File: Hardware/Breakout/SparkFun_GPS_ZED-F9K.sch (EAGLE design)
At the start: 48 parts, among them J1 QWIIC_RIGHT_ANGLE, J4 U.FL, J6 QWIIC_RIGHT_ANGLE, U2 3.3V, U3 UBLOX_ZED_F9K, U4 TRIPLE_BUFFER_74LVC3G07

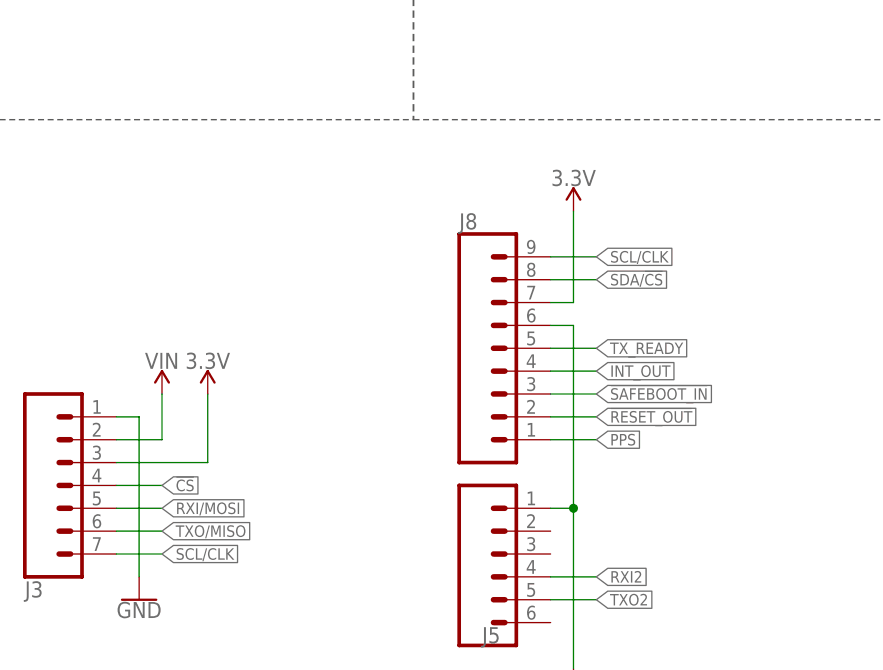
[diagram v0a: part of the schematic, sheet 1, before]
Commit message: Moves buzzard labels to their own folder - updates breakout board with better labeling
* fixes I2C lines being backwards
* Moves D+ and D- lines around
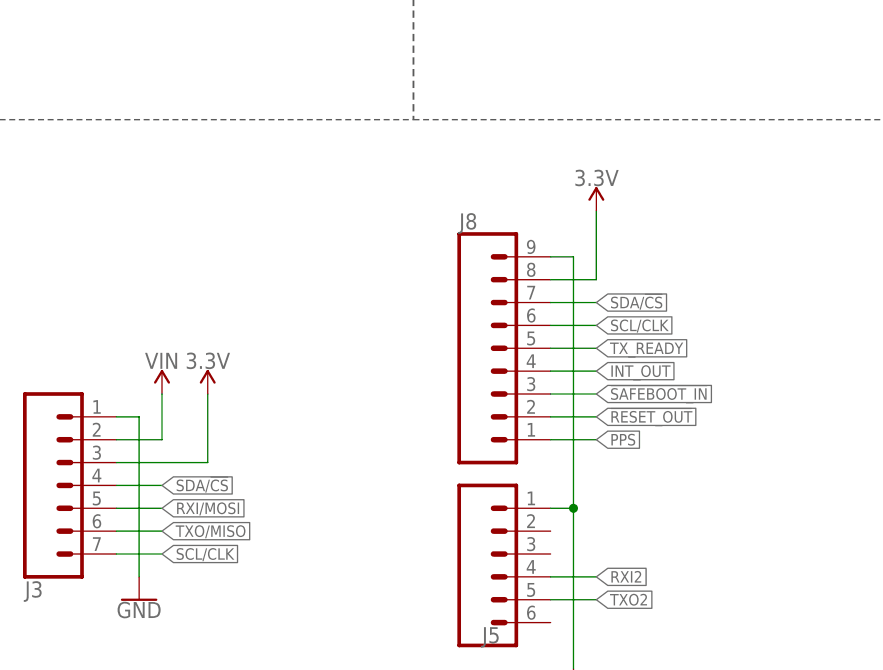
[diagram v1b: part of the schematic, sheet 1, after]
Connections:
- removed net !CS: J3.4
- net 3.3V: now also J8.8; no longer J8.7
- net GND: now also J8.9; no longer J8.6
- net SCL/CLK: now also J8.6; no longer J8.9
- net SDA/!CS: now also J3.4, J8.7; no longer J8.8
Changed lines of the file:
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@@
 <attribute name="NAME" x="345.44" y="122.428" size="1.778" layer="95" font="vector"/>
 </instance>
-<instance part="SUPPLY12" gate="G$1" x="358.14" y="124.46" smashed="yes">
-<attribute name="VALUE" x="358.14" y="127.254" size="1.778" layer="96" align="bottom-center"/>
+<instance part="SUPPLY12" gate="G$1" x="360.68" y="124.46" smashed="yes">
+<attribute name="VALUE" x="360.68" y="127.254" size="1.778" layer="96" align="bottom-center"/>
 </instance>
 <instance part="U4" gate="G$1" x="116.84" y="50.8" smashed="yes">
@@
 <wire x1="358.14" y1="91.44" x2="358.14" y2="73.66" width="0.1524" layer="91"/>
 <pinref part="GND9" gate="1" pin="GND"/>
-<pinref part="J8" gate="J1" pin="6"/>
-<wire x1="355.6" y1="111.76" x2="358.14" y2="111.76" width="0.1524" layer="91"/>
-<wire x1="358.14" y1="111.76" x2="358.14" y2="91.44" width="0.1524" layer="91"/>
+<wire x1="358.14" y1="119.38" x2="358.14" y2="91.44" width="0.1524" layer="91"/>
 <junction x="358.14" y="91.44"/>
+<pinref part="J8" gate="J1" pin="9"/>
+<wire x1="355.6" y1="119.38" x2="358.14" y2="119.38" width="0.1524" layer="91"/>
 </segment>
 <segment>
@@
 </segment>
 <segment>
-<pinref part="J8" gate="J1" pin="7"/>
-<wire x1="355.6" y1="114.3" x2="358.14" y2="114.3" width="0.1524" layer="91"/>
-<wire x1="358.14" y1="114.3" x2="358.14" y2="124.46" width="0.1524" layer="91"/>
 <pinref part="SUPPLY12" gate="G$1" pin="3.3V"/>
+<pinref part="J8" gate="J1" pin="8"/>
+<wire x1="360.68" y1="116.84" x2="360.68" y2="124.46" width="0.1524" layer="91"/>
+<wire x1="355.6" y1="116.84" x2="360.68" y2="116.84" width="0.1524" layer="91"/>
 </segment>
 <segment>
@@
 </segment>
 <segment>
-<pinref part="J8" gate="J1" pin="9"/>
-<wire x1="355.6" y1="119.38" x2="360.68" y2="119.38" width="0.1524" layer="91"/>
-<label x="360.68" y="119.38" size="1.27" layer="95" font="vector" xref="yes"/>
-</segment>
-<segment>
 <pinref part="U3" gate="G$1" pin="SCL/CLK"/>
 <wire x1="106.68" y1="226.06" x2="109.22" y2="226.06" width="0.1524" layer="91"/>
@@
 <label x="312.42" y="86.36" size="1.27" layer="95" font="vector" xref="yes"/>
 <pinref part="J3" gate="J1" pin="7"/>
+</segment>
+<segment>
+<wire x1="355.6" y1="111.76" x2="360.68" y2="111.76" width="0.1524" layer="91"/>
+<label x="360.68" y="111.76" size="1.27" layer="95" font="vector" xref="yes"/>
+<pinref part="J8" gate="J1" pin="6"/>
 </segment>
 </net>
@@
 </segment>
 <segment>
-<pinref part="J8" gate="J1" pin="8"/>
-<wire x1="355.6" y1="116.84" x2="360.68" y2="116.84" width="0.1524" layer="91"/>
-<label x="360.68" y="116.84" size="1.27" layer="95" font="vector" xref="yes"/>
-</segment>
-<segment>
 <pinref part="U3" gate="G$1" pin="SDA/!CS!"/>
 <wire x1="106.68" y1="228.6" x2="109.22" y2="228.6" width="0.1524" layer="91"/>
 <label x="109.22" y="228.6" size="1.27" layer="95" font="vector" xref="yes"/>
+</segment>
+<segment>
+<wire x1="307.34" y1="93.98" x2="312.42" y2="93.98" width="0.1524" layer="91"/>
+<label x="312.42" y="93.98" size="1.27" layer="95" font="vector" xref="yes"/>
+<pinref part="J3" gate="J1" pin="4"/>
+</segment>
+<segment>
+<wire x1="355.6" y1="114.3" x2="360.68" y2="114.3" width="0.1524" layer="91"/>
+<label x="360.68" y="114.3" size="1.27" layer="95" font="vector" xref="yes"/>
+<pinref part="J8" gate="J1" pin="7"/>
 </segment>
 </net>
@@
 </segment>
 </net>
-<net name="!CS" class="0">
-<segment>
-<wire x1="307.34" y1="93.98" x2="312.42" y2="93.98" width="0.1524" layer="91"/>
-<label x="312.42" y="93.98" size="1.27" layer="95" font="vector" xref="yes"/>
-<pinref part="J3" gate="J1" pin="4"/>
-</segment>
-</net>

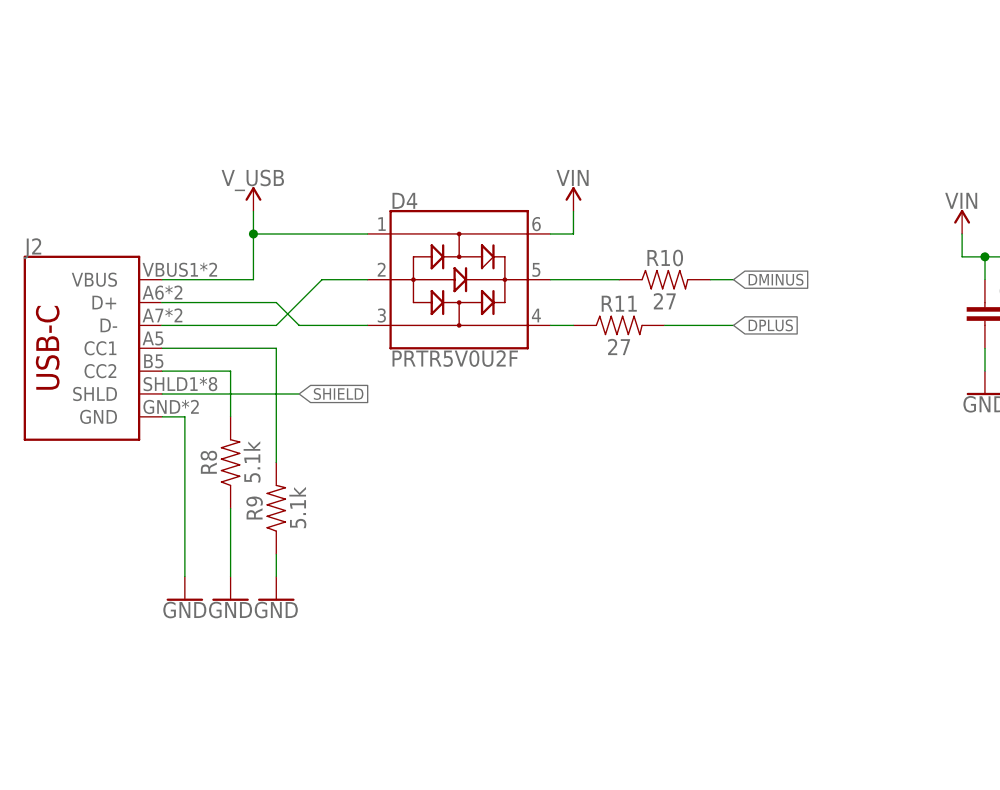
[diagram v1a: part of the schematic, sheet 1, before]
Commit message: Fixes routing for ESD protection IC
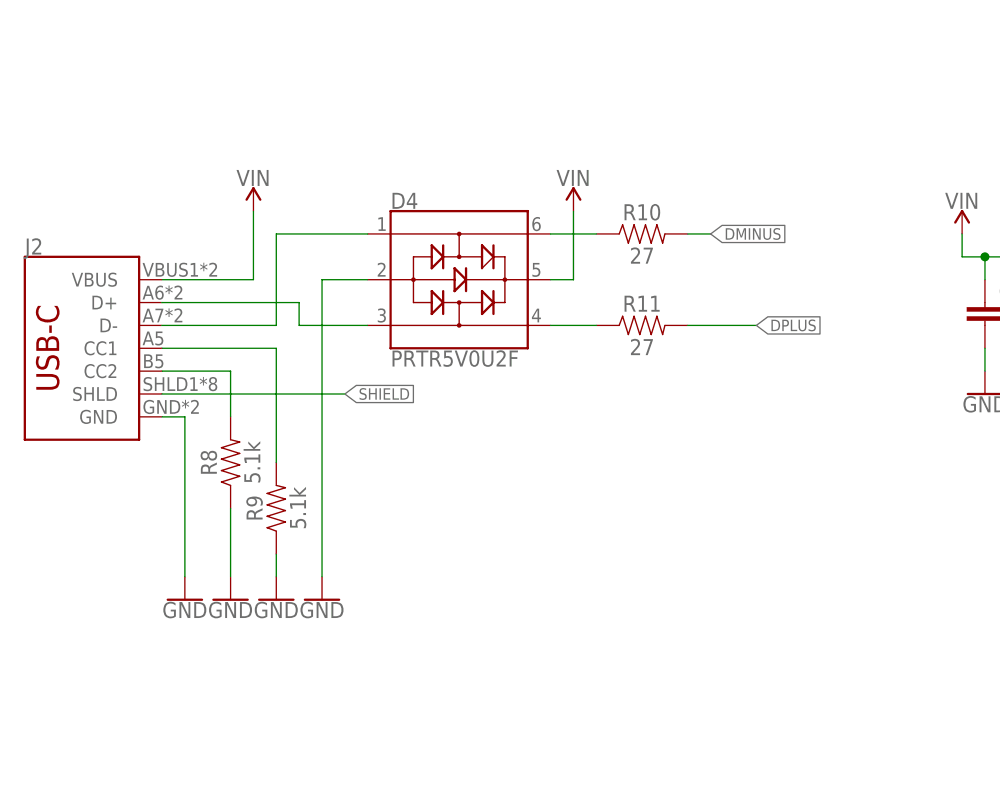
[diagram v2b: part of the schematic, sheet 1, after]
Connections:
- removed net N$16: D4.5, R10.1
- removed net V_USB: D4.1, J2.VBUS
- new net N$9: D4.6, R10.1
- net GND: now also D4.2
- net N$7: now also D4.1; no longer D4.2
- net VIN: now also D4.5, J2.VBUS; no longer D4.6
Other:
- moved on the sheet: R10, R11
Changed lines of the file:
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@@
 <part name="GND5" library="SparkFun-PowerSymbols" deviceset="GND" device=""/>
 <part name="SUPPLY15" library="SparkFun-PowerSymbols" deviceset="3.3V" device=""/>
-<part name="SUPPLY16" library="SparkFun-PowerSymbols" deviceset="V_USB" device=""/>
-<part name="SUPPLY13" library="SparkFun-PowerSymbols" deviceset="VIN" device=""/>
 <part name="SUPPLY10" library="SparkFun-PowerSymbols" deviceset="VIN" device=""/>
 <part name="R5" library="SparkFun-Resistors" deviceset="20OHM" device="-0603-1/10W-1%" value="20"/>
@@
 <part name="LOGO2" library="SparkFun-Aesthetics" deviceset="QWIIC_LOGO" device="_4MM"/>
 <part name="LOGO3" library="SparkFun-Aesthetics" deviceset="OSHW-LOGO" device="M"/>
+<part name="SUPPLY6" library="SparkFun-PowerSymbols" deviceset="VIN" device=""/>
+<part name="GND1" library="SparkFun-PowerSymbols" deviceset="GND" device=""/>
+<part name="SUPPLY13" library="SparkFun-PowerSymbols" deviceset="VIN" device=""/>
 </parts>
 <sheets>
@@
 <attribute name="VALUE" x="213.36" y="215.646" size="1.778" layer="96" align="top-left"/>
 </instance>
-<instance part="R10" gate="G$1" x="243.84" y="223.52" smashed="yes">
-<attribute name="NAME" x="243.84" y="225.044" size="1.778" layer="95" font="vector" align="bottom-center"/>
-<attribute name="VALUE" x="243.84" y="221.996" size="1.778" layer="96" font="vector" align="top-center"/>
-</instance>
-<instance part="R11" gate="G$1" x="238.76" y="218.44" smashed="yes">
-<attribute name="NAME" x="238.76" y="219.964" size="1.778" layer="95" font="vector" align="bottom-center"/>
-<attribute name="VALUE" x="238.76" y="216.916" size="1.778" layer="96" font="vector" align="top-center"/>
+<instance part="R10" gate="G$1" x="241.3" y="228.6" smashed="yes">
+<attribute name="NAME" x="241.3" y="230.124" size="1.778" layer="95" font="vector" align="bottom-center"/>
+<attribute name="VALUE" x="241.3" y="227.076" size="1.778" layer="96" font="vector" align="top-center"/>
+</instance>
+<instance part="R11" gate="G$1" x="241.3" y="218.44" smashed="yes">
+<attribute name="NAME" x="241.3" y="219.964" size="1.778" layer="95" font="vector" align="bottom-center"/>
+<attribute name="VALUE" x="241.3" y="216.916" size="1.778" layer="96" font="vector" align="top-center"/>
 </instance>
 <instance part="R13" gate="G$1" x="203.2" y="30.48" smashed="yes">
@@
 <attribute name="VALUE" x="276.86" y="84.074" size="1.778" layer="96" align="bottom-center"/>
 </instance>
-<instance part="SUPPLY16" gate="G$1" x="198.12" y="231.14" smashed="yes">
-<attribute name="VALUE" x="198.12" y="233.934" size="1.778" layer="96" align="bottom-center"/>
-</instance>
-<instance part="SUPPLY13" gate="G$1" x="233.68" y="231.14" smashed="yes">
-<attribute name="VALUE" x="233.68" y="233.934" size="1.778" layer="96" align="bottom-center"/>
-</instance>
 <instance part="SUPPLY10" gate="G$1" x="276.86" y="228.6" smashed="yes">
 <attribute name="VALUE" x="276.86" y="231.394" size="1.778" layer="96" align="bottom-center"/>
@@
 <instance part="LOGO2" gate="G$1" x="358.14" y="40.64" smashed="yes"/>
 <instance part="LOGO3" gate="G$1" x="332.74" y="45.72" smashed="yes"/>
+<instance part="SUPPLY6" gate="G$1" x="198.12" y="231.14" smashed="yes">
+<attribute name="VALUE" x="198.12" y="233.934" size="1.778" layer="96" align="bottom-center"/>
+</instance>
+<instance part="GND1" gate="1" x="205.74" y="187.96" smashed="yes">
+<attribute name="VALUE" x="205.74" y="187.706" size="1.778" layer="96" align="top-center"/>
+</instance>
+<instance part="SUPPLY13" gate="G$1" x="233.68" y="231.14" smashed="yes">
+<attribute name="VALUE" x="233.68" y="233.934" size="1.778" layer="96" align="bottom-center"/>
+</instance>
 </instances>
 <busses>
@@
 <pinref part="GND22" gate="1" pin="GND"/>
 </segment>
+<segment>
+<pinref part="D4" gate="D1" pin="2"/>
+<wire x1="210.82" y1="223.52" x2="205.74" y2="223.52" width="0.1524" layer="91"/>
+<wire x1="205.74" y1="223.52" x2="205.74" y2="190.5" width="0.1524" layer="91"/>
+<pinref part="GND1" gate="1" pin="GND"/>
+</segment>
 </net>
 <net name="3.3V" class="0">
@@
 <segment>
 <pinref part="J2" gate="J1" pin="SHLD"/>
-<wire x1="187.96" y1="210.82" x2="203.2" y2="210.82" width="0.1524" layer="91"/>
-<label x="203.2" y="210.82" size="1.27" layer="95" font="vector" xref="yes"/>
+<wire x1="187.96" y1="210.82" x2="208.28" y2="210.82" width="0.1524" layer="91"/>
+<label x="208.28" y="210.82" size="1.27" layer="95" font="vector" xref="yes"/>
 </segment>
 </net>
@@
 <segment>
 <pinref part="R10" gate="G$1" pin="2"/>
-<wire x1="248.92" y1="223.52" x2="251.46" y2="223.52" width="0.1524" layer="91"/>
-<label x="251.46" y="223.52" size="1.27" layer="95" font="vector" xref="yes"/>
+<wire x1="246.38" y1="228.6" x2="248.92" y2="228.6" width="0.1524" layer="91"/>
+<label x="248.92" y="228.6" size="1.27" layer="95" font="vector" xref="yes"/>
 </segment>
 <segment>
@@
 <segment>
 <pinref part="R11" gate="G$1" pin="2"/>
-<wire x1="243.84" y1="218.44" x2="251.46" y2="218.44" width="0.1524" layer="91"/>
-<label x="251.46" y="218.44" size="1.27" layer="95" font="vector" xref="yes"/>
+<wire x1="246.38" y1="218.44" x2="254" y2="218.44" width="0.1524" layer="91"/>
+<label x="254" y="218.44" size="1.27" layer="95" font="vector" xref="yes"/>
 </segment>
 <segment>
@@
 </net>
 <net name="VIN" class="0">
-<segment>
-<pinref part="D4" gate="D1" pin="6"/>
-<wire x1="231.14" y1="228.6" x2="233.68" y2="228.6" width="0.1524" layer="91"/>
-<wire x1="233.68" y1="228.6" x2="233.68" y2="231.14" width="0.1524" layer="91"/>
-<pinref part="SUPPLY13" gate="G$1" pin="VIN"/>
-</segment>
 <segment>
 <pinref part="U2" gate="G$1" pin="IN"/>
@@
 <pinref part="SUPPLY4" gate="G$1" pin="VIN"/>
 </segment>
-</net>
-<net name="N$16" class="0">
+<segment>
+<pinref part="J2" gate="J1" pin="VBUS"/>
+<wire x1="198.12" y1="231.14" x2="198.12" y2="223.52" width="0.1524" layer="91"/>
+<wire x1="198.12" y1="223.52" x2="187.96" y2="223.52" width="0.1524" layer="91"/>
+<pinref part="SUPPLY6" gate="G$1" pin="VIN"/>
+</segment>
 <segment>
 <pinref part="D4" gate="D1" pin="5"/>
-<pinref part="R10" gate="G$1" pin="1"/>
-<wire x1="231.14" y1="223.52" x2="238.76" y2="223.52" width="0.1524" layer="91"/>
-</segment>
-</net>
-<net name="N$17" class="0">
-<segment>
-<pinref part="D4" gate="D1" pin="4"/>
-<pinref part="R11" gate="G$1" pin="1"/>
-<wire x1="231.14" y1="218.44" x2="233.68" y2="218.44" width="0.1524" layer="91"/>
+<wire x1="231.14" y1="223.52" x2="233.68" y2="223.52" width="0.1524" layer="91"/>
+<wire x1="233.68" y1="223.52" x2="233.68" y2="231.14" width="0.1524" layer="91"/>
+<pinref part="SUPPLY13" gate="G$1" pin="VIN"/>
 </segment>
 </net>
@@
 <wire x1="106.68" y1="205.74" x2="109.22" y2="205.74" width="0.1524" layer="91"/>
 <label x="109.22" y="205.74" size="1.27" layer="95" font="vector" xref="yes"/>
-</segment>
-</net>
-<net name="V_USB" class="0">
-<segment>
-<pinref part="J2" gate="J1" pin="VBUS"/>
-<pinref part="D4" gate="D1" pin="1"/>
-<wire x1="210.82" y1="228.6" x2="198.12" y2="228.6" width="0.1524" layer="91"/>
-<wire x1="198.12" y1="228.6" x2="198.12" y2="223.52" width="0.1524" layer="91"/>
-<wire x1="198.12" y1="223.52" x2="187.96" y2="223.52" width="0.1524" layer="91"/>
-<junction x="198.12" y="228.6"/>
-<wire x1="198.12" y1="228.6" x2="198.12" y2="231.14" width="0.1524" layer="91"/>
-<pinref part="SUPPLY16" gate="G$1" pin="V_USB"/>
 </segment>
 </net>
@@
 <segment>
 <pinref part="J2" gate="J1" pin="D+"/>
-<wire x1="187.96" y1="220.98" x2="200.66" y2="220.98" width="0.1524" layer="91"/>
+<wire x1="187.96" y1="220.98" x2="203.2" y2="220.98" width="0.1524" layer="91"/>
+<wire x1="203.2" y1="220.98" x2="203.2" y2="218.44" width="0.1524" layer="91"/>
 <pinref part="D4" gate="D1" pin="3"/>
-<wire x1="200.66" y1="220.98" x2="203.2" y2="218.44" width="0.1524" layer="91"/>
 <wire x1="203.2" y1="218.44" x2="210.82" y2="218.44" width="0.1524" layer="91"/>
 </segment>
@@
 <net name="N$7" class="0">
 <segment>
-<pinref part="D4" gate="D1" pin="2"/>
-<wire x1="210.82" y1="223.52" x2="205.74" y2="223.52" width="0.1524" layer="91"/>
-<wire x1="205.74" y1="223.52" x2="200.66" y2="218.44" width="0.1524" layer="91"/>
 <pinref part="J2" gate="J1" pin="D-"/>
 <wire x1="200.66" y1="218.44" x2="187.96" y2="218.44" width="0.1524" layer="91"/>
-</segment>
-</net>
+<wire x1="200.66" y1="218.44" x2="200.66" y2="228.6" width="0.1524" layer="91"/>
+<pinref part="D4" gate="D1" pin="1"/>
+<wire x1="200.66" y1="228.6" x2="210.82" y2="228.6" width="0.1524" layer="91"/>
+</segment>
+</net>
+<net name="N$9" class="0">
+<segment>
+<pinref part="D4" gate="D1" pin="6"/>
+<pinref part="R10" gate="G$1" pin="1"/>
+<wire x1="231.14" y1="228.6" x2="236.22" y2="228.6" width="0.1524" layer="91"/>
+</segment>
+</net>
+<net name="N$10" class="0">
+<segment>
+<pinref part="D4" gate="D1" pin="4"/>
+<pinref part="R11" gate="G$1" pin="1"/>
+<wire x1="231.14" y1="218.44" x2="236.22" y2="218.44" width="0.1524" layer="91"/>
+</segment>
+</net>

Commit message: Updates breakout board with the same parts as the pi hat
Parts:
- removed L1: 3.9NH, SparkFun-Coils:FERRITE_BEAD-120_OHM-0402
- removed U4: TRIPLE_BUFFER_74LVC3G07, classified:TRIPLE_BUFFER_74LVC3G07
- added D3: BLUE, SparkFun-LED:LED-BLUE0603
- added FB1: FERRITE_BEAD-120_OHM-0402, SparkFun-Coils:FERRITE_BEAD-120_OHM-0402
- added GEO: JUMPER-SMT_2_NC_TRACE_SILK, SparkFun-Jumpers:JUMPER-SMT_2_NC_TRACE_SILK
- added R12, R15, R16, R17, R18, R19, R20, R21, R22, R23, R24, R25, R26, R27, R7: 33, SparkFun-Resistors:33OHM-0402-1/10W-1%
- added R28: 1KOHM-0402-1/16W-1%, SparkFun-Resistors:1KOHM-0402-1/16W-1%
- C1: value 0.1uF -> 47pF; device SparkFun-Capacitors:0.1UF-0402-16V-10% -> SparkFun-Capacitors:47PF-0603-50V-5%
- J3: device SparkFun-Connectors:CONN_07NO_SILK -> SparkFun-Connectors:CONN_09NO_SILK
- R5: value 20 -> 10; device SparkFun-Resistors:20OHM-0603-1/10W-1% -> SparkFun-Resistors:10OHM-0603-1/10W-1%
- U3: value UBLOX_ZED_F9K -> UBLOX_ZED_F9R; device classified:UBLOX_ZED_F9K -> classified:UBLOX_ZED_F9R
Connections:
- removed net !RESET_IN: U3.!RESET!, U4.2A
- removed net !RESET_OUT: J8.2, U4.1Y
- removed net !SAFEBOOT_IN: J8.3, U4.3A
- removed net !SAFEBOOT_OUT: U3.!SAFEBOOT!, U4.3Y
- removed net INT_IN: U3.EXTINT, U4.1A
- removed net INT_OUT: J8.4, U4.2Y
- new net !RESET: J8.4, R7.2
- new net !SAFEBOOT: J8.3, R25.2
- new net DIR: J3.8, R27.1
- new net GEOF_STAT: D3.A, R22.2
- new net INT: J8.2, R12.2
- new net N$11: R7.1, U3.!RESET!
- new net N$12: R12.1, U3.EXTINT
- new net N$16: R15.1, U3.SDA/!CS!
- new net N$17: R16.1, U3.SCL/CLK
- new net N$18: R17.1, U3.TX_READY
- new net N$19: R18.1, U3.TX/MISO
- new net N$20: R19.1, U3.RX/MOSI
- new net N$21: R20.1, U3.TX2
- new net N$26: R21.1, U3.RX2
- new net N$27: R22.1, U3.GEO_FENCE_STAT
- new net N$28: R23.1, U3.RTK_STAT
- new net N$29: R24.1, U3.TIMEPULSE
- new net N$30: R25.1, U3.!SAFEBOOT!
- new net N$31: R26.2, U3.WHEEL_TKS
- new net N$32: R27.2, U3.DIR
- new net N$33: GEO.2, R28.1
- new net N$34: D3.C, R28.2
- new net WT: J3.9, R26.1
- net 3.3V: no longer U4.VCC
- net GND: now also GEO.1; no longer U4.GND
- net N$5: now also FB1.2; no longer L1.2
- net PPS: now also R24.2; no longer U3.TIMEPULSE
- net RF_IN: now also FB1.1; no longer L1.1
- net RTK_STAT: now also R23.2; no longer U3.RTK_STAT
- net RXI/MOSI: now also R19.2; no longer U3.RX/MOSI
- net RXI2: now also R21.2; no longer U3.RX2
- net SCL/CLK: now also R16.2; no longer U3.SCL/CLK
- net SDA/!CS: now also R15.2; no longer U3.SDA/!CS!
- net TXO/MISO: now also R18.2; no longer U3.TX/MISO
- net TXO2: now also R20.2; no longer U3.TX2
- net TX_READY: now also R17.2; no longer U3.TX_READY
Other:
- note added: "Dead Reckoning Module - ublox ZED-F9R"
- note removed: "!!!"
- note removed: "ADR Module - ublox ZED-F9P"
- note removed: "I/O Buffer"
- note removed: "Order new parts"
